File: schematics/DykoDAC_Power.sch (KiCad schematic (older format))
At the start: 40 parts, among them J1 AC Input, U1 LT1762-5, U2 LM317, U3 LM337, U4 L7805, U5 78L05, U6 LP5907-3.3, U7 LP5907-3.3

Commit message: pcb update
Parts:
- U2, U3, U4: footprint TO_SOT_Packages_SMD:SOT-223-3_TabPin2 -> TO_SOT_Packages_SMD:TO-263-2
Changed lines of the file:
@@
 F 0 "U4" H 7150 2342 50  0000 C CNN
 F 1 "L7805" H 7150 2251 50  0000 C CNN
-F 2 "TO_SOT_Packages_SMD:SOT-223-3_TabPin2" H 7175 1950 50  0001 L CIN
+F 2 "TO_SOT_Packages_SMD:TO-263-2" H 7175 1950 50  0001 L CIN
 F 3 "http://www.st.com/content/ccc/resource/technical/document/datasheet/41/4f/b3/b0/12/d4/47/88/CD00000444.pdf/files/CD00000444.pdf/jcr:content/translations/en.CD00000444.pdf" H 7150 2050 50  0001 C CNN
 	1    7150 2100
@@
 F 0 "U3" H 3700 2701 50  0000 C CNN
 F 1 "LM337" H 3700 2610 50  0000 C CNN
-F 2 "TO_SOT_Packages_SMD:SOT-223-3_TabPin2" H 3700 2650 50  0001 C CIN
+F 2 "TO_SOT_Packages_SMD:TO-263-2" H 3700 2650 50  0001 C CIN
 F 3 "http://www.ti.com/lit/ds/symlink/lm337-n.pdf" H 3700 2850 50  0001 C CNN
 	1    3700 2850
@@
 F 0 "U2" H 3700 1208 50  0000 C CNN
 F 1 "LM317" H 3700 1299 50  0000 C CNN
-F 2 "TO_SOT_Packages_SMD:SOT-223-3_TabPin2" H 3700 1250 50  0001 C CIN
+F 2 "TO_SOT_Packages_SMD:TO-263-2" H 3700 1250 50  0001 C CIN
 F 3 "http://www.ti.com/lit/ds/symlink/lm337-n.pdf" H 3700 1450 50  0001 C CNN
 	1    3700 1450

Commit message: switch
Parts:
- added SW5: SW_SPDT, Button_Switch_THT:SW_Push_1P2T_Vertical_E-Switch_800UDP8P1A1M6, symbol Switch:SW_SPDT
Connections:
- net GND: now also J1.1 (Pin_1); no longer J1.2 (Pin_2)
- net at F1.2: now also SW5.1 (A); no longer J1.1 (Pin_1)
- new net: J1.2 (Pin_2), SW5.2 (B)
- no-connect marks 0 -> 1
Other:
- moved on the sheet: J1
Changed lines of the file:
@@
 L Connector:Screw_Terminal_01x02 J1
 U 1 1 5C8C0A04
-P 1150 2250
-F 0 "J1" H 1070 2467 50  0000 C CNN
-F 1 "AC Input" H 1070 2376 50  0000 C CNN
-F 2 "Terminal_Blocks:TerminalBlock_Altech_AK300-2_P5.00mm" H 1150 2250 50  0001 C CNN
-F 3 "~" H 1150 2250 50  0001 C CNN
-	1    1150 2250
+P 800 2250
+F 0 "J1" H 720 2467 50  0000 C CNN
+F 1 "AC Input" H 720 2376 50  0000 C CNN
+F 2 "Terminal_Blocks:TerminalBlock_Altech_AK300-2_P5.00mm" H 800 2250 50  0001 C CNN
+F 3 "~" H 800 2250 50  0001 C CNN
+	1    800  2250
 	-1   0    0    -1
 $EndComp
@@
 L power:GND #PWR01
 U 1 1 5C8C1266
-P 1600 2450
-F 0 "#PWR01" H 1600 2200 50  0001 C CNN
-F 1 "GND" H 1605 2277 50  0000 C CNN
-F 2 "" H 1600 2450 50  0001 C CNN
-F 3 "" H 1600 2450 50  0001 C CNN
-	1    1600 2450
-	1    0    0    -1
+P 1150 2150
+F 0 "#PWR01" H 1150 1900 50  0001 C CNN
+F 1 "GND" H 1155 1977 50  0000 C CNN
+F 2 "" H 1150 2150 50  0001 C CNN
+F 3 "" H 1150 2150 50  0001 C CNN
+	1    1150 2150
+	-1   0    0    1
 $EndComp
 $Comp
@@
 	2200 2150 2200 2250
 Wire Wire Line
-	1350 2350 1600 2350
-Wire Wire Line
-	1600 2350 1600 2450
-Wire Wire Line
-	1350 2250 1600 2250
+	1150 2250 1150 2150
 Wire Wire Line
 	1900 2250 2200 2250
@@
 	9850 2700 9400 2700
 Connection ~ 9400 2700
+$Comp
+L Switch:SW_SPDT SW5
+U 1 1 5E682A1D
+P 1350 2350
+F 0 "SW5" H 1350 2635 50  0000 C CNN
+F 1 "SW_SPDT" H 1350 2544 50  0000 C CNN
+F 2 "Button_Switch_THT:SW_Push_1P2T_Vertical_E-Switch_800UDP8P1A1M6" H 1350 2350 50  0001 C CNN
+F 3 "~" H 1350 2350 50  0001 C CNN
+	1    1350 2350
+	1    0    0    -1
+$EndComp
+Wire Wire Line
+	1600 2250 1550 2250
+Wire Wire Line
+	1150 2350 1000 2350
+Wire Wire Line
+	1150 2250 1000 2250
+NoConn ~ 1550 2450
 $EndSCHEMATC

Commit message: update
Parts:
- C14, C15, C64, C65, C9: footprint Capacitors_Tantalum_SMD:CP_Tantalum_Case-A_EIA-3216-18_Reflow -> Capacitor_Tantalum_SMD:CP_EIA-3216-18_Kemet-A
- C49, C7, C8: footprint Capacitors_Tantalum_SMD:CP_Tantalum_Case-D_EIA-7343-31_Reflow -> Capacitor_Tantalum_SMD:CP_EIA-7343-31_Kemet-D
- SW5: value SW_SPDT -> PWR_SWITCH
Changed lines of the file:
@@
 F 0 "C8" H 5068 2546 50  0000 L CNN
 F 1 "100u" H 5068 2455 50  0000 L CNN
-F 2 "Capacitors_Tantalum_SMD:CP_Tantalum_Case-D_EIA-7343-31_Reflow" H 4988 2350 50  0001 C CNN
+F 2 "Capacitor_Tantalum_SMD:CP_EIA-7343-31_Kemet-D" H 4988 2350 50  0001 C CNN
 F 3 "~" H 4950 2500 50  0001 C CNN
 	1    4950 2500
@@
 F 0 "C7" H 5068 1846 50  0000 L CNN
 F 1 "100u" H 5068 1755 50  0000 L CNN
-F 2 "Capacitors_Tantalum_SMD:CP_Tantalum_Case-D_EIA-7343-31_Reflow" H 4988 1650 50  0001 C CNN
+F 2 "Capacitor_Tantalum_SMD:CP_EIA-7343-31_Kemet-D" H 4988 1650 50  0001 C CNN
 F 3 "~" H 4950 1800 50  0001 C CNN
 F 4 "TAJD107K016SNJ " H 4950 1800 50  0001 C CNN "Part"
@@
 F 0 "C9" H 4818 4696 50  0000 L CNN
 F 1 "10u" H 4818 4605 50  0000 L CNN
-F 2 "Capacitors_Tantalum_SMD:CP_Tantalum_Case-A_EIA-3216-18_Reflow" H 4738 4500 50  0001 C CNN
+F 2 "Capacitor_Tantalum_SMD:CP_EIA-3216-18_Kemet-A" H 4738 4500 50  0001 C CNN
 F 3 "~" H 4700 4650 50  0001 C CNN
 F 4 "T491A106K016AT " H 4700 4650 50  0001 C CNN "Part"
@@
 F 0 "C14" H 7668 2396 50  0000 L CNN
 F 1 "10u" H 7668 2305 50  0000 L CNN
-F 2 "Capacitors_Tantalum_SMD:CP_Tantalum_Case-A_EIA-3216-18_Reflow" H 7588 2200 50  0001 C CNN
+F 2 "Capacitor_Tantalum_SMD:CP_EIA-3216-18_Kemet-A" H 7588 2200 50  0001 C CNN
 F 3 "~" H 7550 2350 50  0001 C CNN
 	1    7550 2350
@@
 F 0 "C15" H 7550 4750 50  0000 L CNN
 F 1 "10u" H 7350 4550 50  0000 L CNN
-F 2 "Capacitors_Tantalum_SMD:CP_Tantalum_Case-A_EIA-3216-18_Reflow" H 7588 4500 50  0001 C CNN
+F 2 "Capacitor_Tantalum_SMD:CP_EIA-3216-18_Kemet-A" H 7588 4500 50  0001 C CNN
 F 3 "~" H 7550 4650 50  0001 C CNN
 	1    7550 4650
@@
 F 0 "C64" H 3788 1996 50  0000 L CNN
 F 1 "10u" H 3800 1900 50  0000 L CNN
-F 2 "Capacitors_Tantalum_SMD:CP_Tantalum_Case-A_EIA-3216-18_Reflow" H 3700 1950 50  0001 C CNN
+F 2 "Capacitor_Tantalum_SMD:CP_EIA-3216-18_Kemet-A" H 3700 1950 50  0001 C CNN
 F 3 "~" H 3700 1950 50  0001 C CNN
 	1    3700 1950
@@
 F 0 "C65" H 3788 2396 50  0000 L CNN
 F 1 "10u" H 3800 2300 50  0000 L CNN
-F 2 "Capacitors_Tantalum_SMD:CP_Tantalum_Case-A_EIA-3216-18_Reflow" H 3700 2350 50  0001 C CNN
+F 2 "Capacitor_Tantalum_SMD:CP_EIA-3216-18_Kemet-A" H 3700 2350 50  0001 C CNN
 F 3 "~" H 3700 2350 50  0001 C CNN
 	1    3700 2350
@@
 F 0 "C49" H 9968 2396 50  0000 L CNN
 F 1 "100u" H 9968 2305 50  0000 L CNN
-F 2 "Capacitors_Tantalum_SMD:CP_Tantalum_Case-D_EIA-7343-31_Reflow" H 9888 2200 50  0001 C CNN
+F 2 "Capacitor_Tantalum_SMD:CP_EIA-7343-31_Kemet-D" H 9888 2200 50  0001 C CNN
 F 3 "~" H 9850 2350 50  0001 C CNN
 	1    9850 2350
@@
 U 1 1 5E682A1D
 P 1350 2350
-F 0 "SW5" H 1350 2635 50  0000 C CNN
-F 1 "SW_SPDT" H 1350 2544 50  0000 C CNN
+F 0 "SW5" H 1300 2150 50  0000 C CNN
+F 1 "PWR_SWITCH" H 1350 2050 50  0000 C CNN
 F 2 "Button_Switch_THT:SW_Push_1P2T_Vertical_E-Switch_800UDP8P1A1M6" H 1350 2350 50  0001 C CNN
 F 3 "~" H 1350 2350 50  0001 C CNN

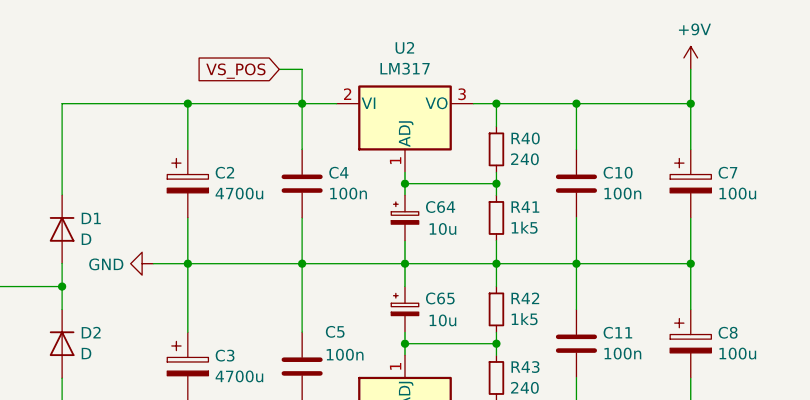
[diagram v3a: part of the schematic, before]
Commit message: lm317 fix
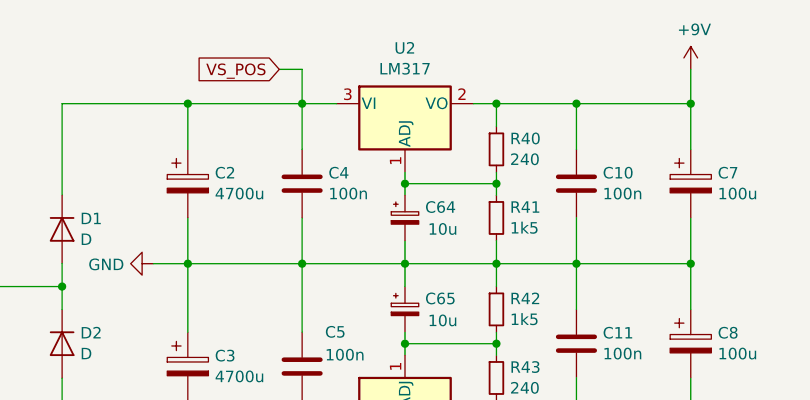
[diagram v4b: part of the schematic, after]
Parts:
- removed U2: LM317, TO_SOT_Packages_SMD:TO-263-2, symbol Regulator_Linear:LM337_SOT223
- added U2: LM317, Package_TO_SOT_SMD:TO-263-2, symbol Regulator_Linear:LM317_3PinPackage
- U3: footprint TO_SOT_Packages_SMD:TO-263-2 -> Package_TO_SOT_SMD:TO-263-2
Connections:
- net +9V: now also U2.2 (VO)
- net VS_POS: now also U2.3 (VI)
- net at C64.1, R40.2, R41.1: now also U2.1 (ADJ)
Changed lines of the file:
@@
 F 0 "U3" H 3700 2701 50  0000 C CNN
 F 1 "LM337" H 3700 2610 50  0000 C CNN
-F 2 "TO_SOT_Packages_SMD:TO-263-2" H 3700 2650 50  0001 C CIN
+F 2 "Package_TO_SOT_SMD:TO-263-2" H 3700 2650 50  0001 C CIN
 F 3 "http://www.ti.com/lit/ds/symlink/lm337-n.pdf" H 3700 2850 50  0001 C CNN
 	1    3700 2850
 	1    0    0    -1
-$EndComp
-$Comp
-L Regulator_Linear:LM337_SOT223 U2
-U 1 1 5E575F0D
-P 3700 1450
-F 0 "U2" H 3700 1208 50  0000 C CNN
-F 1 "LM317" H 3700 1299 50  0000 C CNN
-F 2 "TO_SOT_Packages_SMD:TO-263-2" H 3700 1250 50  0001 C CIN
-F 3 "http://www.ti.com/lit/ds/symlink/lm337-n.pdf" H 3700 1450 50  0001 C CNN
-	1    3700 1450
-	1    0    0    1
 $EndComp
 $Comp
@@
 	1150 2250 1000 2250
 NoConn ~ 1550 2450
+$Comp
+L Regulator_Linear:LM317_3PinPackage U2
+U 1 1 5E73E2F4
+P 3700 1450
+F 0 "U2" H 3700 1692 50  0000 C CNN
+F 1 "LM317" H 3700 1601 50  0000 C CNN
+F 2 "Package_TO_SOT_SMD:TO-263-2" H 3700 1700 50  0001 C CIN
+F 3 "http://www.ti.com/lit/ds/symlink/lm317.pdf" H 3700 1450 50  0001 C CNN
+	1    3700 1450
+	1    0    0    -1
+$EndComp
 $EndSCHEMATC

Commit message: updated fuse
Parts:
- F1: footprint Fuse_Holders_and_Fuses:Fuse_SMD2920 -> kamtar:UNIFuse_SMD2920
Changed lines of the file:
@@
 F 0 "F1" V 1525 2250 50  0000 C CNN
 F 1 "Polyfuse" V 1616 2250 50  0000 C CNN
-F 2 "Fuse_Holders_and_Fuses:Fuse_SMD2920" H 1800 2050 50  0001 L CNN
+F 2 "kamtar:UNIFuse_SMD2920" H 1800 2050 50  0001 L CNN
 F 3 "~" H 1750 2250 50  0001 C CNN
 	1    1750 2250

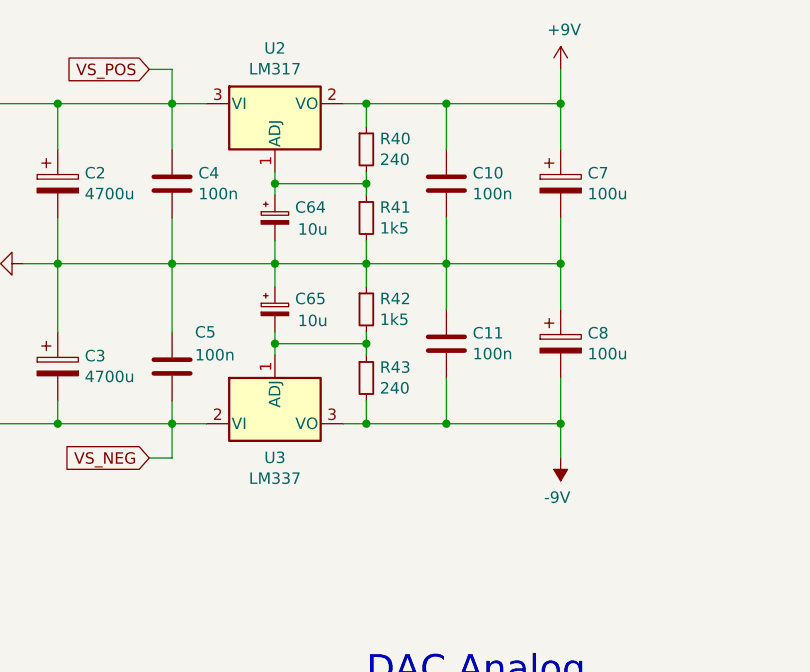
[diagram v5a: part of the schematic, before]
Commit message: ldo change
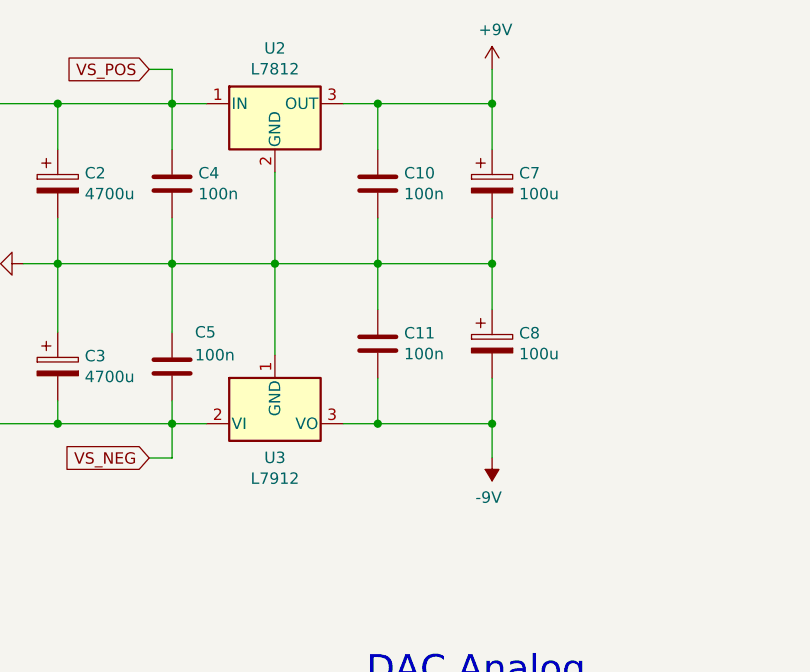
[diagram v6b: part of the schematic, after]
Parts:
- removed C64, C65: 10u, Capacitor_Tantalum_SMD:CP_EIA-3216-18_Kemet-A, symbol Device:CP_Small
- removed R40, R43: 240, Resistors_SMD:R_0603, symbol Device:R_Small
- removed R41, R42: 1k5, Resistors_SMD:R_0603, symbol Device:R_Small
- removed U2: LM317, Package_TO_SOT_SMD:TO-263-2, symbol Regulator_Linear:LM317_3PinPackage
- removed U3: LM337, Package_TO_SOT_SMD:TO-263-2, symbol Regulator_Linear:LM337_SOT223
- added U2: L7812, TO_SOT_Packages_SMD:TO-263-2, symbol Regulator_Linear:L7812
- added U3: L7912, TO_SOT_Packages_SMD:TO-263-2, symbol Regulator_Linear:L7912
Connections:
- net +9V: now also U2.3 (OUT)
- net -9V: now also U3.3 (VO)
- net GND: now also U2.2 (GND), U3.1 (GND)
- net VS_NEG: now also U3.2 (VI)
- net VS_POS: now also U2.1 (IN)
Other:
- moved on the sheet: C10, C11, C7, C8

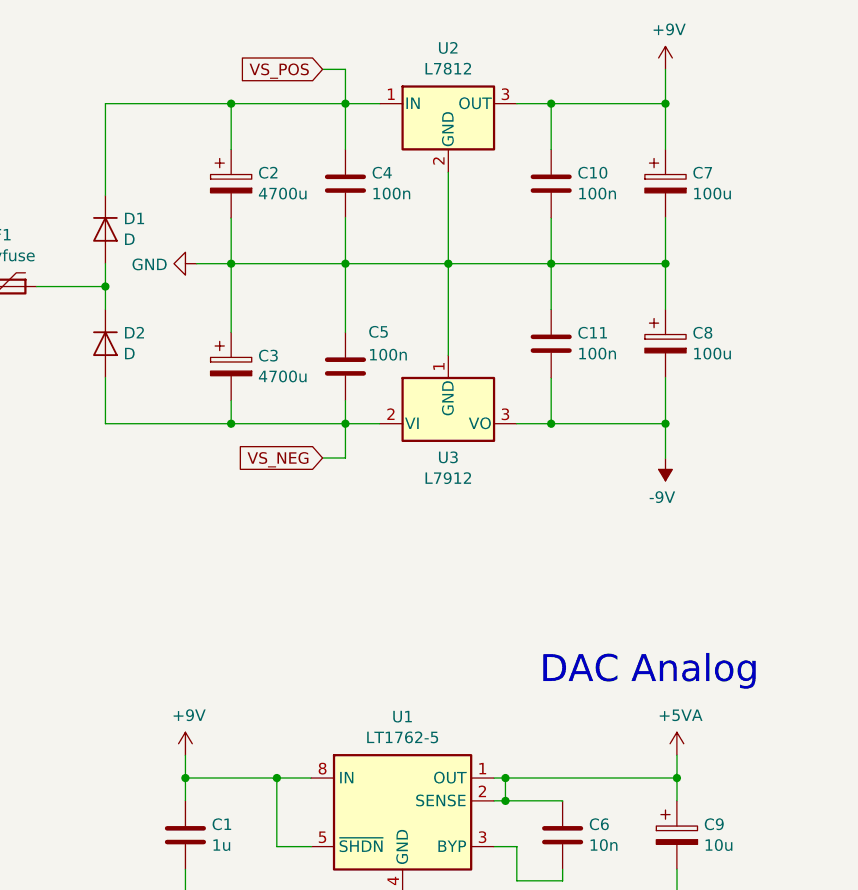
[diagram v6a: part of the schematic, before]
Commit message: 9V -> 12V symbol
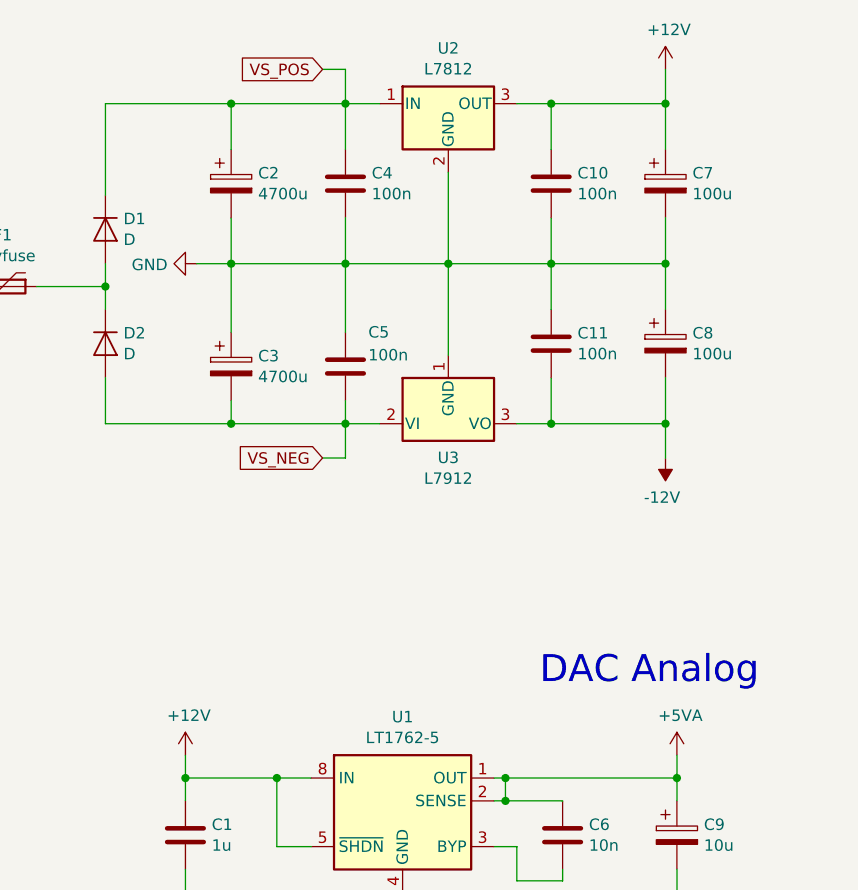
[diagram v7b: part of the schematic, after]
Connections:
- net +9V renamed +12V
- net -9V renamed -12V
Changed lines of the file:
@@
 Text Notes 4100 4000 0    118  ~ 0
 DAC Analog
-$Comp
-L power:+9V #PWR02
-U 1 1 5C8C6769
-P 2550 4300
-F 0 "#PWR02" H 2550 4150 50  0001 C CNN
-F 1 "+9V" H 2565 4473 50  0000 C CNN
-F 2 "" H 2550 4300 50  0001 C CNN
-F 3 "" H 2550 4300 50  0001 C CNN
-	1    2550 4300
-	1    0    0    -1
-$EndComp
 Text Notes 7250 6900 0    236  ~ 0
 Power supply block
@@
 Wire Wire Line
 	3250 3000 3250 2850
-$Comp
-L power:+9V #PWR052
-U 1 1 5E6DDA48
-P 4650 1300
-F 0 "#PWR052" H 4650 1150 50  0001 C CNN
-F 1 "+9V" H 4665 1473 50  0000 C CNN
-F 2 "" H 4650 1300 50  0001 C CNN
-F 3 "" H 4650 1300 50  0001 C CNN
-	1    4650 1300
-	1    0    0    -1
-$EndComp
 Wire Wire Line
 	4650 1300 4650 1450
 Connection ~ 4650 1450
-$Comp
-L power:-9V #PWR067
-U 1 1 5E6E6C4A
-P 4650 3000
-F 0 "#PWR067" H 4650 2875 50  0001 C CNN
-F 1 "-9V" H 4665 3173 50  0000 C CNN
-F 2 "" H 4650 3000 50  0001 C CNN
-F 3 "" H 4650 3000 50  0001 C CNN
-	1    4650 3000
-	-1   0    0    1
-$EndComp
 Connection ~ 4650 2850
 Wire Wire Line
@@
 Wire Wire Line
 	4150 2150 3700 2150
+$Comp
+L power:+12V #PWR?
+U 1 1 5E6CE0CD
+P 4650 1300
+F 0 "#PWR?" H 4650 1150 50  0001 C CNN
+F 1 "+12V" H 4665 1473 50  0000 C CNN
+F 2 "" H 4650 1300 50  0001 C CNN
+F 3 "" H 4650 1300 50  0001 C CNN
+	1    4650 1300
+	1    0    0    -1
+$EndComp
+$Comp
+L power:-12V #PWR?
+U 1 1 5E6CE56D
+P 4650 3000
+F 0 "#PWR?" H 4650 3100 50  0001 C CNN
+F 1 "-12V" H 4665 3173 50  0000 C CNN
+F 2 "" H 4650 3000 50  0001 C CNN
+F 3 "" H 4650 3000 50  0001 C CNN
+	1    4650 3000
+	-1   0    0    1
+$EndComp
+$Comp
+L power:+12V #PWR?
+U 1 1 5E6D4F49
+P 2550 4300
+F 0 "#PWR?" H 2550 4150 50  0001 C CNN
+F 1 "+12V" H 2565 4473 50  0000 C CNN
+F 2 "" H 2550 4300 50  0001 C CNN
+F 3 "" H 2550 4300 50  0001 C CNN
+	1    2550 4300
+	1    0    0    -1
+$EndComp
 $EndSCHEMATC

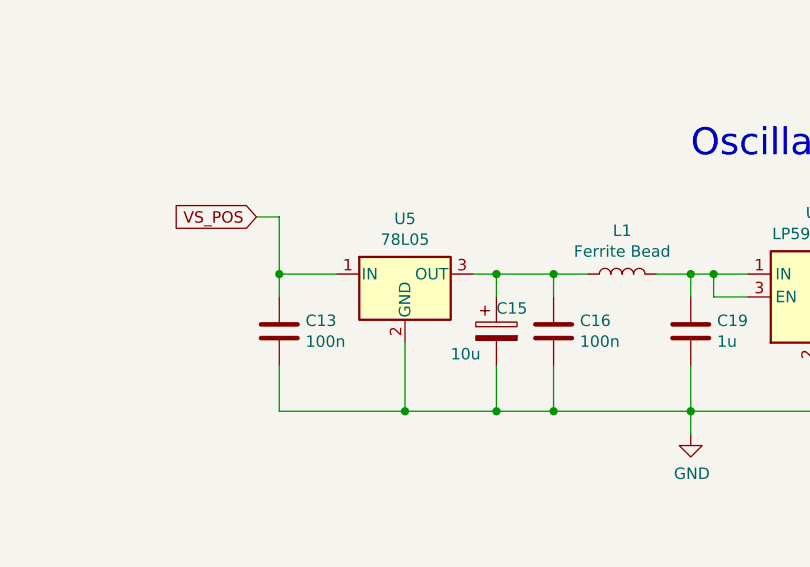
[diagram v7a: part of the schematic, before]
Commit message: PRODUCTION - REV.B - rotated 5Vreg. fixed 78l05, fixed wrong polygon
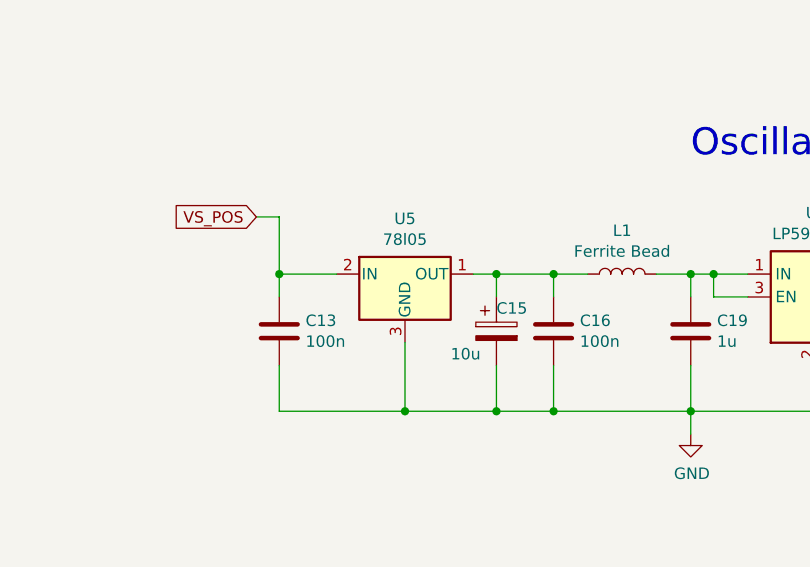
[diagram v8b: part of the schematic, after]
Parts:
- removed U5: 78L05, TO_SOT_Packages_SMD:SOT-23, symbol Regulator_Linear:L7805
- added U5: 78l05, TO_SOT_Packages_SMD:SOT-23, symbol kamtar:78l05
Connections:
- net GND: now also U5.3 (GND)
- net VS_POS: now also U5.2 (IN)
- net at C15.1, C16.1, L1.1: now also U5.1 (OUT)
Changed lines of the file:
@@
 	9400 5000 8950 5000
 Connection ~ 8950 5000
-$Comp
-L Regulator_Linear:L7805 U5
-U 1 1 5CFE5010
-P 7150 4400
-F 0 "U5" H 7150 4642 50  0000 C CNN
-F 1 "78L05" H 7150 4551 50  0000 C CNN
-F 2 "TO_SOT_Packages_SMD:SOT-23" H 7175 4250 50  0001 L CIN
-F 3 "http://www.st.com/content/ccc/resource/technical/document/datasheet/41/4f/b3/b0/12/d4/47/88/CD00000444.pdf/files/CD00000444.pdf/jcr:content/translations/en.CD00000444.pdf" H 7150 4350 50  0001 C CNN
-	1    7150 4400
-	1    0    0    -1
-$EndComp
 Connection ~ 9400 4400
 Text Notes 8400 3900 0    118  ~ 0
@@
 	4150 2150 3700 2150
 $Comp
-L power:+12V #PWR?
+L power:+12V #PWR0103
 U 1 1 5E6CE0CD
 P 4650 1300
-F 0 "#PWR?" H 4650 1150 50  0001 C CNN
+F 0 "#PWR0103" H 4650 1150 50  0001 C CNN
 F 1 "+12V" H 4665 1473 50  0000 C CNN
 F 2 "" H 4650 1300 50  0001 C CNN
@@
 $EndComp
 $Comp
-L power:-12V #PWR?
+L power:-12V #PWR0105
 U 1 1 5E6CE56D
 P 4650 3000
-F 0 "#PWR?" H 4650 3100 50  0001 C CNN
+F 0 "#PWR0105" H 4650 3100 50  0001 C CNN
 F 1 "-12V" H 4665 3173 50  0000 C CNN
 F 2 "" H 4650 3000 50  0001 C CNN
@@
 $EndComp
 $Comp
-L power:+12V #PWR?
+L power:+12V #PWR0106
 U 1 1 5E6D4F49
 P 2550 4300
-F 0 "#PWR?" H 2550 4150 50  0001 C CNN
+F 0 "#PWR0106" H 2550 4150 50  0001 C CNN
 F 1 "+12V" H 2565 4473 50  0000 C CNN
 F 2 "" H 2550 4300 50  0001 C CNN
@@
 	1    0    0    -1
 $EndComp
+$Comp
+L kamtar:78l05 U5
+U 1 1 5E735AE7
+P 7150 4400
+F 0 "U5" H 7150 4642 50  0000 C CNN
+F 1 "78l05" H 7150 4551 50  0000 C CNN
+F 2 "TO_SOT_Packages_SMD:SOT-23" H 7175 4250 50  0001 L CIN
+F 3 "http://www.st.com/content/ccc/resource/technical/document/datasheet/41/4f/b3/b0/12/d4/47/88/CD00000444.pdf/files/CD00000444.pdf/jcr:content/translations/en.CD00000444.pdf" H 7150 4350 50  0001 C CNN
+	1    7150 4400
+	1    0    0    -1
+$EndComp
